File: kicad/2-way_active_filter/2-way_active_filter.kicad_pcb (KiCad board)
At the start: 2 copper layers, 0 parts

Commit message: New commit.
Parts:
- added C1: 2.2 мк, CAPACITOR_MKP4_27_5_32x11, F.Cu at (188.6, 154.3)
- added C10: 4700мк 35В, CAPACITOR_10_D22, F.Cu at (222.2, 101.0)
- added C11: 0.1 мк, SMD0805, F.Cu at (192.4, 50.2)
- added C12: 0.1 мк, SMD0805, F.Cu at (206.4, 53.3)
- added C13: 0.1 мк, SMD0805, F.Cu at (196.8, 60.3)
- added C14: 22 п, SMD0805, F.Cu at (201.9, 53.3)
- added C15: 22 п, SMD0805, F.Cu at (201.9, 57.1)
- added C16: 47мк 25В, CAPACITOR_CD263_2.54_D6.3, F.Cu at (119.4, 117.5)
- added C17: 47мк 25В, CAPACITOR_CD263_2.54_D6.3, F.Cu at (119.4, 105.4)
- added C18: 0.1 мк, SMD0805, F.Cu at (215.3, 63.5)
- added C19: 0.1 мк, SMD0805, F.Cu at (196.8, 63.5)
- added C2: 2.2 мк, CAPACITOR_MKP4_27_5_32x11, F.Cu at (188.6, 140.3)
- added C20: 22 п, SMD0805, F.Cu at (210.8, 50.2)
- added C21: 22 п, SMD0805, F.Cu at (215.3, 50.2)
- added C22: 0.047 мк, CAPACITOR_FKP2_5_7x6.5, F.Cu at (236.9, 18.4)
- added C23: 0.047 мк, CAPACITOR_FKP2_5_7x6.5, F.Cu at (236.9, 67.3)
- added C24: 0.047 мк, CAPACITOR_FKP2_5_7x6.5, F.Cu at (236.9, 57.8)
- added C25: 0.047 мк, CAPACITOR_FKP2_5_7x6.5, F.Cu at (236.9, 48.3)
- added C26: 0.1 мк, SMD0805, F.Cu at (215.3, 57.1)
- added C27: 0.1 мк, SMD0805, F.Cu at (192.4, 53.3)
- added C28: 0.047 мк, CAPACITOR_FKP2_5_7x6.5, F.Cu at (236.9, 28.6)
- added C29: 0.047 мк, CAPACITOR_FKP2_5_7x6.5, F.Cu at (236.9, 38.7)
- added C3: 2.2 мк, CAPACITOR_MKP4_27_5_32x11, F.Cu at (188.6, 111.8)
- added C30: 22 п, SMD0805, F.Cu at (192.4, 60.3)
- added C31: 22 п, SMD0805, F.Cu at (192.4, 57.1)
- added C32: 2.2 мк, CAPACITOR_MKP4_27_5_32x11, F.Cu at (188.6, 126.4)
- added C33: 2.2 мк, CAPACITOR_MKP4_27_5_32x11, F.Cu at (188.6, 97.2)
- added C34: 220 п, SMD0805, F.Cu at (215.3, 53.3)
- added C35: 220 п, SMD0805, F.Cu at (192.4, 63.5)
- added C36: 0.1 мк, SMD0805, F.Cu at (196.8, 57.1)
- added C37: 0.1 мк, SMD0805, F.Cu at (210.8, 60.3)
- added C38: 220 п, SMD0805, F.Cu at (206.4, 63.5)
- added C39: 220 п, SMD0805, F.Cu at (210.8, 63.5)
- added C4: 220 п, SMD0805, F.Cu at (201.9, 50.2)
- added C40: 0.1 мк, SMD0805, F.Cu at (196.8, 53.3)
- added C41: 0.1 мк, SMD0805, F.Cu at (196.8, 50.2)
- added C42: 22 п, SMD0805, F.Cu at (201.9, 63.5)
- added C43: 22 п, SMD0805, F.Cu at (206.4, 60.3)
- added C44: 22 п, SMD0805, F.Cu at (201.9, 60.3)
- added C5: 220 п, SMD0805, F.Cu at (210.8, 57.1)
- added C6: 220 п, SMD0805, F.Cu at (206.4, 57.1)
- added C7: 220 п, SMD0805, F.Cu at (215.3, 60.3)
- added C8: 0.1 мк, SMD0805, F.Cu at (210.8, 53.3)
- added C9: 4700мк 35В, CAPACITOR_10_D22, F.Cu at (222.9, 125.1)
- added DA1: L7815CV, TO220_VERT_POZ, F.Cu at (83.8, 95.9)
- added DA2: L7915CV, TO220_VERT_POZ, F.Cu at (73.7, 95.9)
- added DA3: LME49720MA, SOIC8, F.Cu at (262.3, 111.1)
- added DA4: LME49720MA, SOIC8, F.Cu at (270.5, 100.3)
- added DA5: LME49740MA, SOIC16, F.Cu at (248.3, 111.1)
- added DA6: LME49740MA, SOIC16, F.Cu at (248.3, 100.3)
- added DA7: LME49720MA, SOIC8, F.Cu at (262.3, 100.3)
- added FU1: 0.1 А, FU_PTF15B, F.Cu at (99.7, 133.3)
- added R1: 22 к, SMD0805, F.Cu at (149.2, 57.1)
- added R10: 10 к, SMD0805, F.Cu at (162.6, 50.8)
- added R11: 10 к, SMD0805, F.Cu at (167.0, 50.8)
- added R12: 10 к, SMD0805, F.Cu at (158.1, 57.1)
- added R13: 10 к, SMD0805, F.Cu at (149.2, 50.8)
- added R14: 30 к, SMD0805, F.Cu at (153.7, 54.0)
- added R15: 10 к, SMD0805, F.Cu at (158.1, 66.7)
- added R16: 1 к, SMD0805, F.Cu at (144.8, 69.8)
- added R17: 30 к, SMD0805, F.Cu at (149.2, 66.7)
- added R18: 50 к, Electron_3296W, F.Cu at (247.7, 70.5)
- added R19: 50 к, Electron_3296W, F.Cu at (247.7, 78.7)
- added R2: 22 к, SMD0805, F.Cu at (162.6, 54.0)
- added R20: 50 к, Electron_3296W, F.Cu at (247.7, 62.2)
- added R21: 1 к, SMD0805, F.Cu at (149.2, 69.8)
- added R22: 1 к, SMD0805, F.Cu at (140.3, 69.8)
- added R23: 120 к, SMD0805, F.Cu at (162.6, 69.8)
- added R24: 50 к, Electron_3296W, F.Cu at (247.7, 35.6)
- added R25: 30 к, SMD0805, F.Cu at (158.1, 69.8)
- added R26: 1 к, SMD0805, F.Cu at (153.7, 69.8)
- added R27: 50 к, Electron_3296W, F.Cu at (247.7, 53.3)
- added R28: 1 к, SMD0805, F.Cu at (167.0, 66.7)
- added R29: 50 к, Electron_3296W, F.Cu at (261.6, 18.4)
- added R3: 22 к, SMD0805, F.Cu at (135.3, 54.0)
- added R30: 50 к, Electron_3296W, F.Cu at (247.7, 18.4)
- added R31: 10 к, SMD0805, F.Cu at (153.7, 66.7)
- added R32: 1 к, SMD0805, F.Cu at (162.6, 66.7)
- added R33: 10 к, SMD0805, F.Cu at (144.8, 66.7)
- added R34: 10 к, SMD0805, F.Cu at (140.3, 66.7)
- added R35: 10 к, SMD0805, F.Cu at (135.3, 57.1)
- added R36: 50 к, Electron_3296W, F.Cu at (261.6, 26.0)
- added R37: 50 к, Electron_3296W, F.Cu at (261.6, 35.6)
- added R38: 10, SMD0805, F.Cu at (167.0, 69.8)
- added R39: 10, SMD0805, F.Cu at (135.3, 50.8)
- added R4: 10, SMD0805, F.Cu at (153.7, 50.8)
- added R40: 10, SMD0805, F.Cu at (167.0, 54.0)
- added R41: 10, SMD0805, F.Cu at (158.1, 54.0)
- added R42: 0, SMD0805, F.Cu at (140.3, 63.5)
- added R43: 10, SMD0805, F.Cu at (140.3, 60.3)
- added R44: 10, SMD0805, F.Cu at (140.3, 54.0)
- added R45: 10, SMD0805, F.Cu at (140.3, 57.1)
- added R46: 10, SMD0805, F.Cu at (144.8, 63.5)
- added R47: 10 к, SMD0805, F.Cu at (144.8, 60.3)
- added R48: 10 к, SMD0805, F.Cu at (140.3, 50.8)
- added R49: 50 к, Electron_3296W, F.Cu at (247.7, 44.5)
- added R5: 220, SMD0805, F.Cu at (206.4, 50.2)
- added R50: 50 к, Electron_3296W, F.Cu at (247.7, 26.0)
- added R51: 10 к, SMD0805, F.Cu at (144.8, 54.0)
- added R52: 10 к, SMD0805, F.Cu at (167.0, 63.5)
- added R53: 30 к, SMD0805, F.Cu at (144.8, 50.8)
- added R54: 30 к, SMD0805, F.Cu at (144.8, 57.1)
- added R55: 4.7, SMD0805, F.Cu at (167.0, 60.3)
- added R56: 4.7, SMD0805, F.Cu at (162.6, 60.3)
- added R57: 4.7, SMD0805, F.Cu at (162.6, 63.5)
- added R58: 4.7, SMD0805, F.Cu at (158.1, 63.5)
- added R59: 4.7, SMD0805, F.Cu at (153.7, 63.5)
- added R6: 220, SMD0805, F.Cu at (162.6, 57.1)
- added R60: 4.7, SMD0805, F.Cu at (149.2, 63.5)
- added R61: 4.7, SMD0805, F.Cu at (158.1, 60.3)
- added R62: 4.7, SMD0805, F.Cu at (153.7, 60.3)
- added R63: 4.7, SMD0805, F.Cu at (149.2, 60.3)
- added R64: 4.7, SMD0805, F.Cu at (167.0, 57.1)
- added R7: 220, SMD0805, F.Cu at (149.2, 54.0)
- added R8: 10, SMD0805, F.Cu at (158.1, 50.8)
- added R9: 10 к, SMD0805, F.Cu at (153.7, 57.1)
- added TV1: BVEI 481 0120, BVEI_481_1120, F.Cu at (41.9, 116.8)
- added VD1: SR1100, DO-41, F.Cu at (44.5, 88.3)
- added VD2: SR1100, DO-41, F.Cu at (44.5, 103.5)
- added VD3: SR1100, DO-41, F.Cu at (44.5, 93.3)
- added VD4: SR1100, DO-41, F.Cu at (44.5, 98.4)
- added XS1: WF-3, WF-3, F.Cu at (161.9, 34.3)
- added XS10: WF-4, WF-4, F.Cu at (163.2, 18.4)
- added XS11: WF-4, WF-4, F.Cu at (163.2, 26.7)
- added XS12: WF-4, WF-4, F.Cu at (151.1, 26.7)
- added XS13: DG126-5.0-03P-14, DG126-5.0-03P-14, F.Cu at (104.1, 95.9)
- added XS14: DG126-5.0-03P-14, DG126-5.0-03P-14, F.Cu at (104.1, 106.7)
- added XS15: DG126-5.0-03P-14, DG126-5.0-03P-14, F.Cu at (104.1, 85.1)
- added XS2: WF-4, WF-4, F.Cu at (151.1, 34.3)
- added XS3: WF-3, WF-3, F.Cu at (174.6, 18.4)
- added XS4: DG126-5.0-02P-14, DG126-5.0-02P-14, F.Cu at (99.7, 148.6)
- added XS5: WF-5, WF-5, F.Cu at (149.9, 18.4)
- added XS6: PLS-3, PIN_ARRAY_3x1, F.Cu at (223.5, 16.5)
- added XS7: PLS-2, PIN_ARRAY_2x1, F.Cu at (222.2, 35.6)
- added XS8: PLS-2, PIN_ARRAY_2x1, F.Cu at (222.2, 29.2)
- added XS9: PLS-3, PIN_ARRAY_3x1, F.Cu at (223.5, 22.9)
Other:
- net class Default: clearance 0.254 -> 0.25; trace_width 0.254 -> 0.25; via_dia 1.19888 -> 1.2; via_drill 0.59944 -> 0.6
- rule trace_clearance: 0.254 -> 0.25
- rule trace_min: 0.254 -> 0.25
- rule via_min_drill: 0.508 -> 0.5
- rule via_min_size: 0.889 -> 0.6

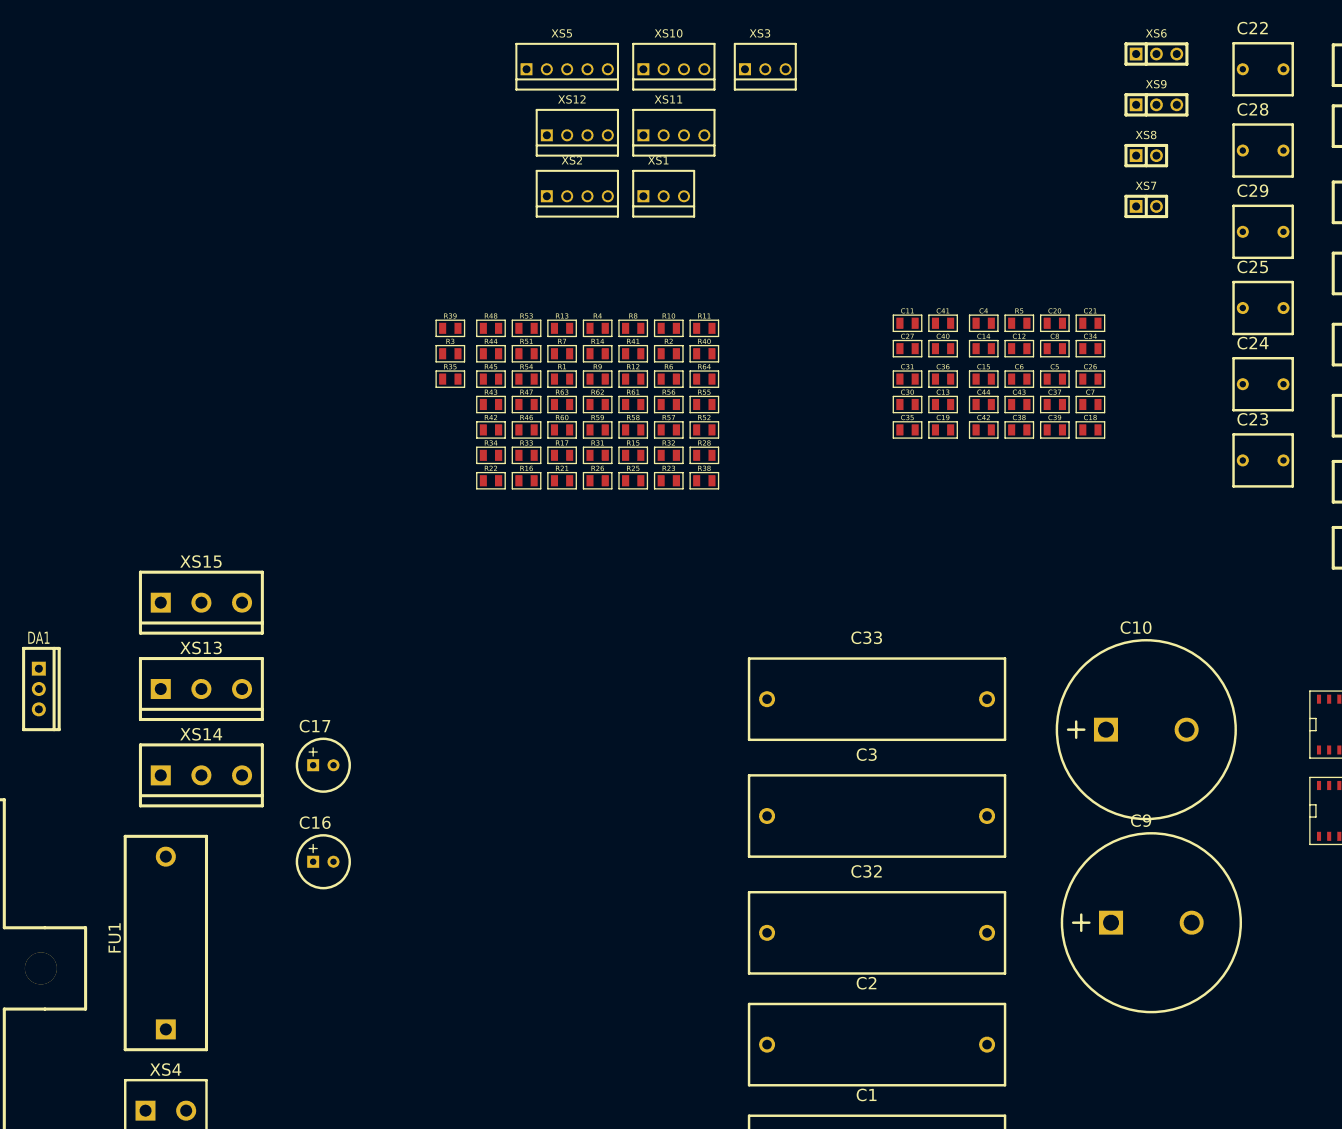
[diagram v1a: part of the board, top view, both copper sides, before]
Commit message: 2-way active filter.
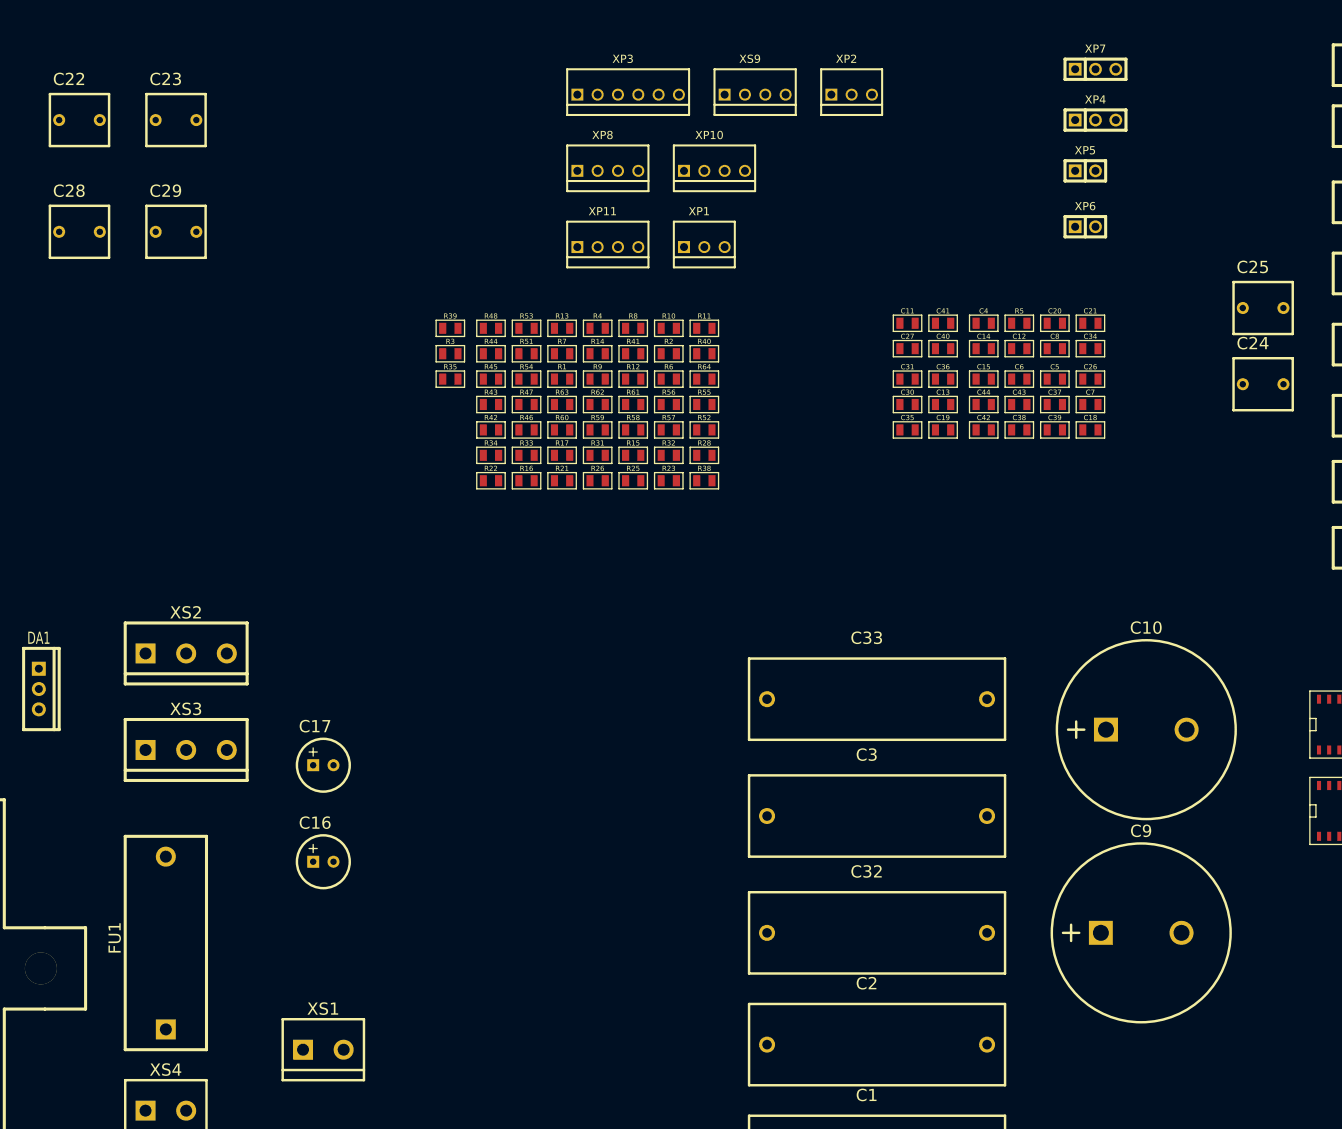
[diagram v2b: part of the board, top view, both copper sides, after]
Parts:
- removed XS10, XS11, XS12: WF-4, WF-4
- removed XS13, XS14, XS15: DG126-5.0-03P-14, DG126-5.0-03P-14
- removed XS5: WF-5, WF-5
- removed XS6: PLS-3, PIN_ARRAY_3x1
- removed XS7, XS8: PLS-2, PIN_ARRAY_2x1
- added XP1: WF-3, WF-3, F.Cu at (167.0, 40.6)
- added XP10: WF-4, WF-4, F.Cu at (168.3, 31.1)
- added XP11: WF-4, WF-4, F.Cu at (154.9, 40.6)
- added XP2: WF-3, WF-3, F.Cu at (185.4, 21.6)
- added XP3: WF-6, WF-6, F.Cu at (157.5, 21.6)
- added XP4: PLS-3, PIN_ARRAY_3x1, F.Cu at (215.9, 24.8)
- added XP5: PLS-2, PIN_ARRAY_2x1, F.Cu at (214.6, 31.1)
- added XP6: PLS-2, PIN_ARRAY_2x1, F.Cu at (214.6, 38.1)
- added XP7: PLS-3, PIN_ARRAY_3x1, F.Cu at (215.9, 18.4)
- added XP8: WF-4, WF-4, F.Cu at (154.9, 31.1)
- XS1: value WF-3 -> DG126-5.0-02P-14; footprint WF-3 -> DG126-5.0-02P-14
- XS2: value WF-4 -> DG126-5.0-03P-14; footprint WF-4 -> DG126-5.0-03P-14
- XS3: value WF-3 -> DG126-5.0-03P-14; footprint WF-3 -> DG126-5.0-03P-14
- XS9: value PLS-3 -> WF-4; footprint PIN_ARRAY_3x1 -> WF-4
- moved C28 148.3 mm to (88.9, 38.7)
- moved C22 148.1 mm to (88.9, 24.8)
- moved C23 142.4 mm to (101.0, 24.8)
- moved C29 135.9 mm to (101.0, 38.7)
- moved XS1 114.9 mm to (119.4, 141.0)
- moved XS3 111.7 mm to (102.2, 103.5)
- moved XS2 75.2 mm to (102.2, 91.4)
- moved XS9 50.2 mm to (173.4, 21.6)
- moved C9 1.80 mm to (221.6, 126.4)
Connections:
- C1 pad 1: N-0000021 -> N-0000022
- C16 pad 1: N-0000074 -> N-0000075
- C16 pad 2: N-0000086 (its old number) -> N-0000087
- C17 pad 1: N-0000086 (its old number) -> N-0000087
- C17 pad 2: N-0000072 (its old number) -> N-0000073
- C18 pad 1: N-0000074 -> N-0000075
- C18 pad 2: N-0000086 (its old number) -> N-0000087
- C19 pad 1: N-0000086 (its old number) -> N-0000087
- C19 pad 2: N-0000072 (its old number) -> N-0000073
- C2 pad 1: N-0000020 (its old number) -> N-0000021
- C22 pad 2: N-0000022 -> N-0000024
- C28 pad 1: N-0000026 (its old number) -> N-0000027
- C28 pad 2: N-0000027 -> N-0000035
- C29 pad 1: N-0000023 (its old number) -> N-0000025
- C3 pad 1: N-0000073 -> N-0000074
- C33 pad 1: N-0000027 -> N-0000035
- DA1 pad 3: N-0000074 -> N-0000075
- DA2 pad 3: N-0000072 (its old number) -> N-0000073
- DA3 pad 1: N-0000033 (its old number) -> N-0000032
- DA3 pad 2: N-0000033 (its old number) -> N-0000032
- DA5 pad 12: N-0000023 (its old number) -> N-0000025
- DA5 pad 13: N-0000027 -> N-0000035
- DA5 pad 14: N-0000027 -> N-0000035
- DA5 pad 8: N-0000022 -> N-0000024
- DA5 pad 9: N-0000022 -> N-0000024
- FU1 pad 1: N-0000035 -> N-000006
- R28 pad 1: N-0000022 -> N-0000024
- R29 pad 2: N-0000026 (its old number) -> N-0000027
- R29 pad 3: N-0000026 (its old number) -> N-0000027
- R30 pad 1: N-0000026 (its old number) -> N-0000027
- R32 pad 2: N-0000023 (its old number) -> N-0000025
- R35 pad 2: N-0000027 -> N-0000035
- R4 pad 2: N-0000057 (its old number) -> N-0000058
- R41 pad 2: N-000002 (its old number) -> N-000003
- R42 pad 2: N-0000033 (its old number) -> N-0000032
- R49 pad 3: N-0000058 -> N-0000045
- R50 pad 3: N-0000033 (its old number) -> N-0000046
- TV1 pad 6: N-0000045 -> N-0000043
- XS1 pad 1: N-0000073 -> N-000006
- XS1 pad 2: /GND -> N-0000043
- XS2 pad 1: N-0000057 (its old number) -> N-0000075
- XS2 pad 2: /GND -> N-0000087
- XS2 pad 3: /GND -> N-0000073
- XS3 pad 1: N-0000021 -> /+15V
- XS3 pad 3: N-0000020 (its old number) -> /-15V
- XS9 pad 1: N-0000022 -> N-000003
- XS9 pad 2: N-0000026 (its old number) -> /GND
- XS9 pad 3: N-0000023 (its old number) -> /GND

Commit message: Add new version 2-way active filter.
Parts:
- removed XS4: DG126-5.0-02P-14, DG126-5.0-02P-14
- added 1_PIN: P***, 1_pin, F.Cu at (92.5, 85.5)
- added 1_PIN: P***, 1_pin, F.Cu at (182.9, 45.8)
- added 1_PIN: P***, 1_pin, F.Cu at (91.4, 45.3)
- added 1_PIN: P***, 1_pin, F.Cu at (182.9, 86.0)
- added 1_PIN: P***, 1_pin, F.Cu at (185.2, 142.4)
- added 1_PIN: P***, 1_pin, F.Cu at (93.6, 146.0)
- added 1_PIN: P***, 1_pin, F.Cu at (92.5, 100.5)
- added 1_PIN: P***, 1_pin, F.Cu at (185.2, 99.8)
- added C45: 0.047 мк, CAPACITOR_FKP2_5_7x6.5, F.Cu at (153.7, 46.0)
- added C46: 0.047 мк, CAPACITOR_FKP2_5_7x6.5, F.Cu at (176.8, 46.0)
- added C47: 0.047 мк, CAPACITOR_FKP2_5_7x6.5, F.Cu at (184.7, 53.8)
- added C48: 0.047 мк, CAPACITOR_FKP2_5_7x6.5, F.Cu at (177.5, 53.8)
- C11, C12, C13, C14, C15, C20, C21, C26, C27, C30, C31, C34, C35, C36, C37, C38, C39, C4, C40, C41, C42, C43, C44, C5, C6, C7, C8, DA3, DA4, DA7, R1, R10, R11, R12, R13, R14, R15, R16, R17, R2, R21, R22, R23, R25, R26, R28, R3, R31, R32, R33, R34, R35, R38, R39, R4, R40, R41, R42, R43, R44, R45, R46, R47, R48, R5, R51, R52, R53, R54, R55, R56, R57, R58, R59, R6, R60, R61, R62, R63, R64, R7, R8, R9: moved to B.Cu
- C32, C33: value 2.2 мк -> 0.047 мк; footprint CAPACITOR_MKP4_27_5_32x11 -> CAPACITOR_FKP2_5_7x6.5
- DA1, DA2: footprint TO220_VERT_POZ -> TO220_RAD_16.5x15
- DA5, DA6: footprint SOIC16 -> SOIC14; moved to B.Cu
- moved DA3 164.0 mm to (102.6, 73.7), turned to 90 degrees
- moved R50 143.3 mm to (113.3, 75.9), turned to 270 degrees
- moved R49 134.2 mm to (114.3, 59.9), turned to 90 degrees
- moved DA7 126.0 mm to (143.0, 59.7), turned to 270 degrees
- moved R36 124.8 mm to (153.7, 88.6), turned to 90 degrees
- moved DA6 124.5 mm to (127.5, 70.1), turned to 90 degrees
- moved DA2 124.2 mm to (196.8, 111.8)
- moved DA4 123.5 mm to (149.4, 76.2), turned to 90 degrees
- moved C7 119.7 mm to (97.0, 79.0)
- moved DA1 117.5 mm to (196.8, 128.0)
- moved VD3 115.9 mm to (157.2, 119.9), turned to 90 degrees
- moved VD1 112.7 mm to (152.7, 119.9), turned to 90 degrees
- moved C22 110.0 mm to (184.7, 79.0), turned to 90 degrees
- moved C1 109.9 mm to (122.2, 66.8), turned to 270 degrees
- moved R19 107.2 mm to (141.2, 66.3)
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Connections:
- C10 pad 1: /GND -> /AGND
- C16 pad 2: N-0000087 -> /AGND
- C17 pad 1: N-0000087 -> /AGND
- C18 pad 2: N-0000087 -> /AGND
- C19 pad 1: N-0000087 -> /AGND
- C20 pad 2: N-0000059 -> N-0000079
- C24 pad 2: N-0000077 (its old number) -> N-0000065
- C25 pad 2: N-0000082 (its old number) -> N-0000067
- C28 pad 1: N-0000027 (its old number) -> /CAP1
- C28 pad 2: N-0000035 (its old number) -> /CAP2
- C29 pad 1: N-0000025 (its old number) -> /CAP3
- C30 pad 2: N-000005 (its old number) -> N-0000021
- C31 pad 1: N-0000036 -> N-0000057
- C31 pad 2: N-000001 (its old number) -> N-0000020
- C32 pad 1: N-000001 (its old number) -> /CAP1
- C32 pad 2: N-000009 (its old number) -> /CAP2
- C33 pad 1: N-0000035 (its old number) -> /CAP1
- C33 pad 2: N-0000010 (its old number) -> /CAP2
- C9 pad 2: /GND -> /AGND
- DA1 pad 2: /GND -> /AGND
- DA2 pad 1: /GND -> /AGND
- DA3 pad 1: N-0000032 (its old number) -> N-0000059
- DA3 pad 2: N-0000032 (its old number) -> N-0000059
- DA4 pad 3: N-0000044 (its old number) -> N-0000036
- DA5 pad 1: N-0000077 (its old number) -> N-0000020
- DA5 pad 12: N-0000025 (its old number) -> /CAP3
- DA5 pad 13: N-0000035 (its old number) -> /CAP2
- DA5 pad 14: N-0000035 (its old number) -> /CAP2
- DA5 pad 2: N-0000082 (its old number) -> N-0000057
- DA5 pad 3: N-0000028 (its old number) -> N-0000021
- DA5 pad 5: N-000005 (its old number) -> N-0000063
- DA5 pad 6: N-0000036 -> N-0000067
- DA5 pad 7: N-000001 (its old number) -> N-0000065
- DA6 pad 14: N-0000059 -> N-0000079
- R14 pad 2: N-0000059 -> N-0000079
- R23 pad 2: N-0000028 (its old number) -> N-0000063
- R25 pad 1: N-0000028 (its old number) -> N-0000063
- R26 pad 2: N-0000082 (its old number) -> N-0000067
- R27 pad 2: N-0000077 (its old number) -> N-0000065
- R27 pad 3: N-0000077 (its old number) -> N-0000065
- R29 pad 2: N-0000027 (its old number) -> /CAP1
- R29 pad 3: N-0000027 (its old number) -> /CAP1
- R30 pad 1: N-0000027 (its old number) -> /CAP1
- R31 pad 1: N-0000077 (its old number) -> N-0000065
- R31 pad 2: N-000005 (its old number) -> N-0000021
- R32 pad 2: N-0000025 (its old number) -> /CAP3
- R33 pad 1: N-000005 (its old number) -> N-0000021
- R34 pad 1: N-0000036 -> N-0000057
- R34 pad 2: N-000001 (its old number) -> N-0000020
- R35 pad 1: N-0000036 -> N-0000057
- R35 pad 2: N-0000035 (its old number) -> /CAP2
- R36 pad 3: N-000009 (its old number) -> N-0000020
- R37 pad 3: N-0000010 (its old number) -> /CAP2
- R42 pad 2: N-0000032 (its old number) -> N-0000059
- R43 pad 1: N-0000067 -> N-0000024
- R44 pad 1: N-0000068 (its old number) -> N-0000023
- R49 pad 3: N-0000045 (its old number) -> N-0000081
- R50 pad 3: N-0000046 (its old number) -> N-0000078
- TV1 pad 11: /GND -> /AGND
- TV1 pad 8: /GND -> /AGND
- XP11 pad 1: N-0000067 -> N-0000023
- XP11 pad 4: N-0000068 (its old number) -> N-0000024
- XP3 pad 1: N-0000032 (its old number) -> /GND
- XP3 pad 2: N-0000046 (its old number) -> N-0000036
- XP3 pad 3: N-0000059 -> N-0000081
- XP3 pad 4: N-0000045 (its old number) -> N-0000079
- XP3 pad 5: N-0000044 (its old number) -> N-0000078
- XP3 pad 6: /GND -> N-0000059
- XP6 pad 1: N-0000082 (its old number) -> N-0000067
- XP6 pad 2: N-0000077 (its old number) -> N-0000065
- XP7 pad 2: N-0000027 (its old number) -> /CAP1
- XP7 pad 3: N-0000025 (its old number) -> /CAP3
- XS2 pad 2: N-0000087 -> /AGND
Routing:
- net /GND: track 0.00 -> 191.5 mm, vias 0 -> 14
- net /-15V: track 0.00 -> 120.8 mm, vias 0 -> 4
- net /+15V: track 0.00 -> 112.4 mm, vias 0 -> 6
- net /AGND: track 0.00 -> 104.9 mm, vias 0 -> 2
- net N-0000040: track 0.00 -> 85.4 mm
- net /CAP3: track 0.00 -> 64.7 mm, vias 0 -> 1
- net /CAP2: track 0.00 -> 64.1 mm, vias 0 -> 1
- net N-0000051: track 0.00 -> 61.3 mm
- net N-0000041: track 0.00 -> 60.6 mm
- net N-0000044: track 0.00 -> 57.2 mm
- net /CAP1: track 0.00 -> 53.9 mm
- net N-0000039: track 0.00 -> 53.7 mm
- net N-0000077: track 0.00 -> 50.7 mm
- net N-0000060: track 0.00 -> 48.7 mm, vias 0 -> 2
- net N-0000071: track 0.00 -> 46.9 mm, vias 0 -> 1
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- added copper zone on B.Cu, net /AGND
- added copper zone on B.Cu, net /GND
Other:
- board outline added: 112 x 109.6 mm
